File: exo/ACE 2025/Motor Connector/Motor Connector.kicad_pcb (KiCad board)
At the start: 2 copper layers, 62 x 44 mm, 4 parts, among them J1 RJ45, J2 Conn_01x04

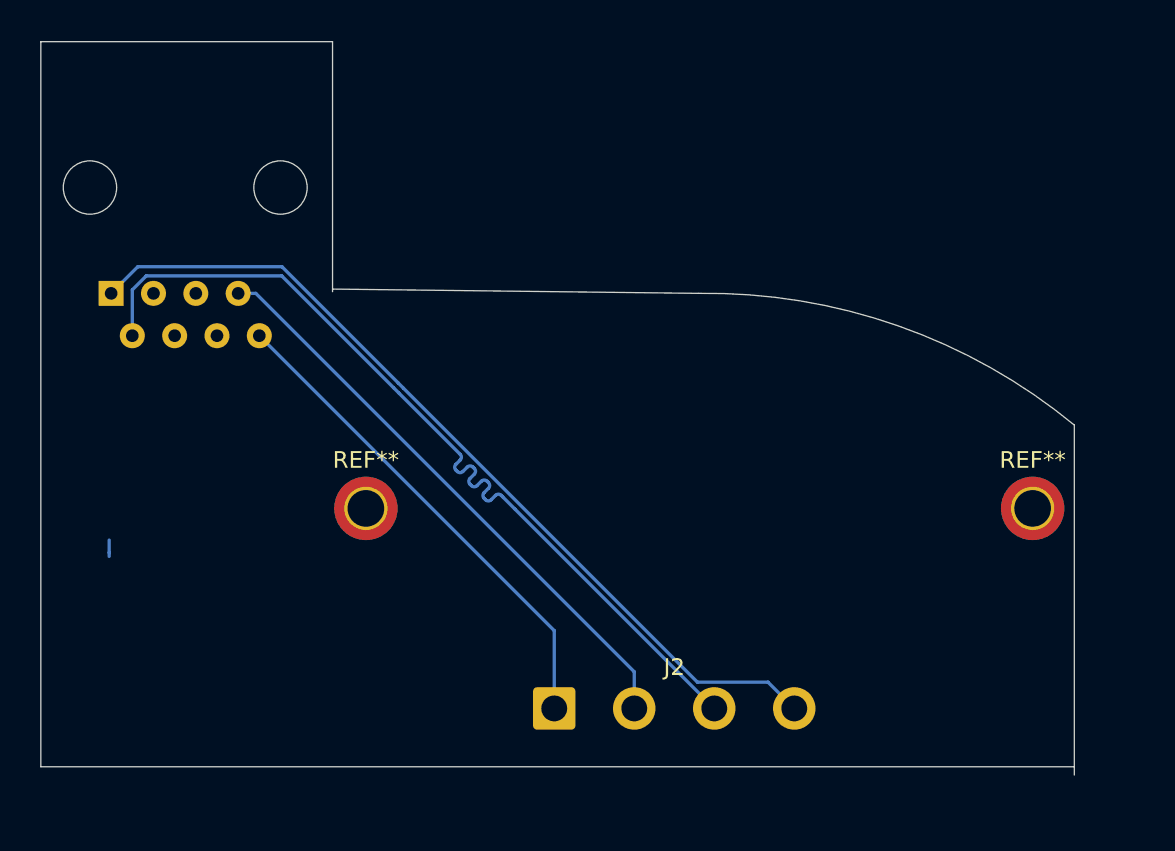
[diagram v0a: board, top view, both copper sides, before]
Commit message: push connecteur FIX
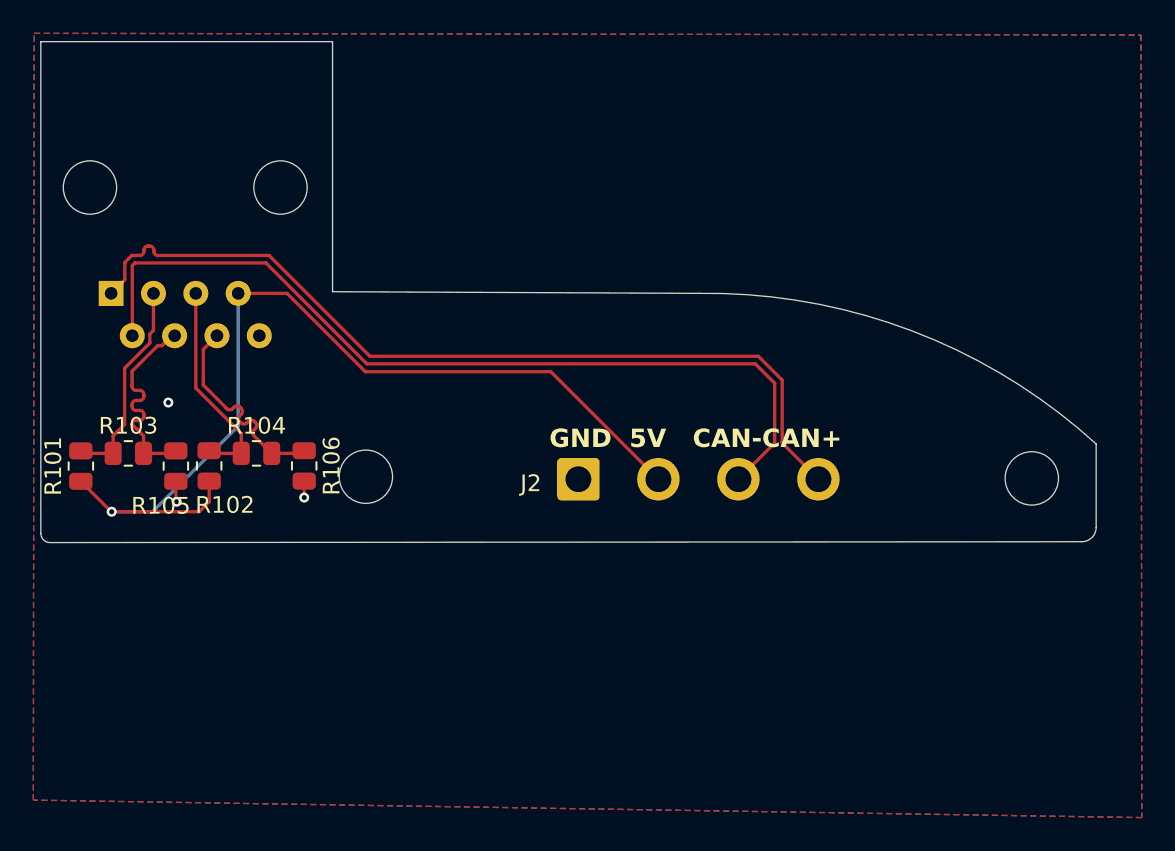
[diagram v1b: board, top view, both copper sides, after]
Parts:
- removed the REF** at (69.5, 51.0)
- removed the REF** at (109.5, 51.0)
- added ?: , , F.Cu at (69.5, 49.1)
- added R101: 600, Resistor_SMD:R_0805_2012Metric, F.Cu at (52.4, 48.5)
- added R102: 600, Resistor_SMD:R_0805_2012Metric, F.Cu at (60.1, 48.5)
- added R103: 110, Resistor_SMD:R_0805_2012Metric, F.Cu at (55.2, 47.7)
- added R104: 110, Resistor_SMD:R_0805_2012Metric, F.Cu at (62.9, 47.7)
- added R105: 600, Resistor_SMD:R_0805_2012Metric, F.Cu at (58.1, 48.5)
- added R106: 600, Resistor_SMD:R_0805_2012Metric, F.Cu at (65.8, 48.5)
- added REF**: MountingHole_3.2mm_M3, MountingHole:MountingHole_3.2mm_M3, F.Cu at (109.5, 49.2)
- moved J2 13.8 mm to (82.2, 49.2)
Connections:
- J1 pad 3: unconnected-(J1-Pad3) -> /SCL+
- J1 pad 4: unconnected-(J1-Pad4) -> /SCL-
- J1 pad 5: unconnected-(J1-Pad5) -> /SDA+
- J1 pad 6: unconnected-(J1-Pad6) -> /SDA-
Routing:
- net /GND: track 29.7 -> 2.23 mm, vias 0 -> 3
- net /5V: track 36.3 -> 57.5 mm, vias 0 -> 1
- net /SDA+: track 0.00 -> 12.7 mm
- net /SDA-: track 0.00 -> 12.7 mm
- net /SCL+: track 0.00 -> 12.6 mm
- net /SCL-: track 0.00 -> 12.6 mm
- added copper zone on B.Cu, net /GND
- added copper zone on F.Cu, net /GND
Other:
- board size 62 x 44 mm -> 63.3 x 30 mm
- board text added: "GND 5V CAN-CAN+"
